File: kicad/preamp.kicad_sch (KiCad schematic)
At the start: 14 parts, among them Q1 MMBF5457, Q2 MMBF5457

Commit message: Datasheet footprints, floor-plan placement, headless autoroute (144/145, DRC 0)
PCB-AUDIT s1 fixes with datasheet-derived project footprints:
- TO-220-5_Vertical_P1.70mm_LM1875 (TI NDH0005D): 1.45 mm pads on the 1.1 mm
  drill -> 0.175 mm annular (was 0.0875, 5 DRC errors); pad-local 0.2 mm clearance
- Bridge_KBP_P3.81mm (Diodes DS39310 KBP404G-KBP410G, pins + ~ ~ -); bridge
  symbol renumbered to the physical order; errata #3 updated (KBU needs a swap)
- value-aware CP/R sizing (real can sizes for 4700/2200/1000 uF, 5 W / 1 W
  resistors, fat pads on the 0R speaker return); Part 4 wire pads for all
  off-board wiring (2.0 mm/1.2 mm signal, 3.0 mm/1.5 mm speaker + transformer)
- VRAW/AC1/AC2 moved into the HighCurrent net class (errata #11)

gen_pcb.py now places to the Part 5 floor plan: balanced columns (Input/Preamp
with Tone stacked below | Reverb/Trem/MRB | Power Amp | PSU), signal order inside
zones with serpentine shelves, LM1875/LM317 on the top edge with the 10 mm
keep-out, wiring edge along the bottom, 4x M3 holes, two locked 0.9 mm escape
stubs off the LM1875 pins 4/5 (a 1.5/2.5 mm trace cannot enter a 1.70 mm pitch).
DRC before routing: 0 errors, 0 warnings.

route_board.py: pcbnew DSN export -> Freerouting -> SES import -> pour refill.
Freerouting 2.1.0 ignores every pass/timeout limit in CLI mode and only writes
output at 0 unrouted (and its MT router crashed), so the script drives 1.9.0
under xvfb-run and injects autoroute_settings (bottom layer 6x cost, via 80) so
the GND pour stays whole. Committed board: 144/145 connections routed, 0 DRC
violations (--severity-all), 26 vias, 351 mm on the bottom vs 3.7 m on top; the
one open PA_OUT link (blocked by R_bias1) is documented as a GUI finish.

Chassis-fit figure corrected: the old 48-53 % / 82-90 % densities counted hidden
text boxes; text-less it is ~33 % on 190x115 and ~56 % on 155x90.

Docs: PCB-NOTES/PCB-AUDIT rewritten, README, CHANGELOG, errata #3/#11,
SOURCES (package drawings), Part 10, kicad RE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
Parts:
- C_s1, C_s2: footprint Capacitor_THT:CP_Radial_D8.0mm_P3.50mm -> Capacitor_THT:CP_Radial_D5.0mm_P2.00mm
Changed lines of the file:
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@@
     (pin "1")
     (pin "2")
-    (instances (project "cambridge_reverb" (path "/942ea049-022a-4522-9155-9a031f6385fe" (reference "C_in_pre") (unit 1))))
+    (instances (project "cambridge_reverb" (path "/0294f5b1-e3f0-489d-af89-80fb9260e410" (reference "C_in_pre") (unit 1))))
   )
   (wire (pts (xy 116.84 121.91999999999999) (xy 114.3 121.91999999999999)) (stroke (width 0) (type default)))
@@
     (pin "1")
     (pin "2")
-    (instances (project "cambridge_reverb" (path "/942ea049-022a-4522-9155-9a031f6385fe" (reference "R_g1") (unit 1))))
+    (instances (project "cambridge_reverb" (path "/0294f5b1-e3f0-489d-af89-80fb9260e410" (reference "R_g1") (unit 1))))
   )
   (wire (pts (xy 116.84 152.4) (xy 114.3 152.4)) (stroke (width 0) (type default)))
@@
     (pin "1")
     (pin "3")
-    (instances (project "cambridge_reverb" (path "/942ea049-022a-4522-9155-9a031f6385fe" (reference "Q1") (unit 1))))
+    (instances (project "cambridge_reverb" (path "/0294f5b1-e3f0-489d-af89-80fb9260e410" (reference "Q1") (unit 1))))
   )
   (wire (pts (xy 165.1 132.07999999999998) (xy 162.56 132.07999999999998)) (stroke (width 0) (type default)))
@@
     (pin "1")
     (pin "2")
-    (instances (project "cambridge_reverb" (path "/942ea049-022a-4522-9155-9a031f6385fe" (reference "R_d1") (unit 1))))
+    (instances (project "cambridge_reverb" (path "/0294f5b1-e3f0-489d-af89-80fb9260e410" (reference "R_d1") (unit 1))))
   )
   (wire (pts (xy 167.64 101.6) (xy 165.1 101.6)) (stroke (width 0) (type default)))
@@
     (pin "1")
     (pin "2")
-    (instances (project "cambridge_reverb" (path "/942ea049-022a-4522-9155-9a031f6385fe" (reference "R_s1") (unit 1))))
+    (instances (project "cambridge_reverb" (path "/0294f5b1-e3f0-489d-af89-80fb9260e410" (reference "R_s1") (unit 1))))
   )
   (wire (pts (xy 167.64 172.72) (xy 165.1 172.72)) (stroke (width 0) (type default)))
@@
     (property "Reference" "C_s1" (at 214.62999999999997 165.1 0) (effects (font (size 1.27 1.27)) (justify left)))
     (property "Value" "10uF/25V" (at 214.62999999999997 167.64 0) (effects (font (size 1.27 1.27)) (justify left)))
-    (property "Footprint" "Capacitor_THT:CP_Radial_D8.0mm_P3.50mm" (at 212.08999999999997 172.72 0) (effects (font (size 1.27 1.27)) hide))
+    (property "Footprint" "Capacitor_THT:CP_Radial_D5.0mm_P2.00mm" (at 212.08999999999997 172.72 0) (effects (font (size 1.27 1.27)) hide))
     (pin "1")
     (pin "2")
-    (instances (project "cambridge_reverb" (path "/942ea049-022a-4522-9155-9a031f6385fe" (reference "C_s1") (unit 1))))
+    (instances (project "cambridge_reverb" (path "/0294f5b1-e3f0-489d-af89-80fb9260e410" (reference "C_s1") (unit 1))))
   )
   (wire (pts (xy 207.01 172.72) (xy 204.46999999999997 172.72)) (stroke (width 0) (type default)))
@@
     (pin "1")
     (pin "2")
-    (instances (project "cambridge_reverb" (path "/942ea049-022a-4522-9155-9a031f6385fe" (reference "C_cpl12") (unit 1))))
+    (instances (project "cambridge_reverb" (path "/0294f5b1-e3f0-489d-af89-80fb9260e410" (reference "C_cpl12") (unit 1))))
   )
   (wire (pts (xy 207.01 132.07999999999998) (xy 204.46999999999997 132.07999999999998)) (stroke (width 0) (type default)))
@@
     (pin "1")
     (pin "2")
-    (instances (project "cambridge_reverb" (path "/942ea049-022a-4522-9155-9a031f6385fe" (reference "R_g2") (unit 1))))
+    (instances (project "cambridge_reverb" (path "/0294f5b1-e3f0-489d-af89-80fb9260e410" (reference "R_g2") (unit 1))))
   )
   (wire (pts (xy 207.01 157.48) (xy 204.46999999999997 157.48)) (stroke (width 0) (type default)))
@@
     (pin "1")
     (pin "3")
-    (instances (project "cambridge_reverb" (path "/942ea049-022a-4522-9155-9a031f6385fe" (reference "Q2") (unit 1))))
+    (instances (project "cambridge_reverb" (path "/0294f5b1-e3f0-489d-af89-80fb9260e410" (reference "Q2") (unit 1))))
   )
   (wire (pts (xy 250.19 132.07999999999998) (xy 247.64999999999998 132.07999999999998)) (stroke (width 0) (type default)))
@@
     (pin "1")
     (pin "2")
-    (instances (project "cambridge_reverb" (path "/942ea049-022a-4522-9155-9a031f6385fe" (reference "R_d2") (unit 1))))
+    (instances (project "cambridge_reverb" (path "/0294f5b1-e3f0-489d-af89-80fb9260e410" (reference "R_d2") (unit 1))))
   )
   (wire (pts (xy 252.72999999999996 101.6) (xy 250.19 101.6)) (stroke (width 0) (type default)))
@@
     (pin "1")
     (pin "2")
-    (instances (project "cambridge_reverb" (path "/942ea049-022a-4522-9155-9a031f6385fe" (reference "C_pres") (unit 1))))
+    (instances (project "cambridge_reverb" (path "/0294f5b1-e3f0-489d-af89-80fb9260e410" (reference "C_pres") (unit 1))))
   )
   (wire (pts (xy 252.72999999999996 172.72) (xy 250.19 172.72)) (stroke (width 0) (type default)))
@@
     (pin "1")
     (pin "2")
-    (instances (project "cambridge_reverb" (path "/942ea049-022a-4522-9155-9a031f6385fe" (reference "R_s2") (unit 1))))
+    (instances (project "cambridge_reverb" (path "/0294f5b1-e3f0-489d-af89-80fb9260e410" (reference "R_s2") (unit 1))))
   )
   (wire (pts (xy 292.09999999999997 157.48) (xy 289.56 157.48)) (stroke (width 0) (type default)))
@@
     (property "Reference" "C_s2" (at 299.72 173.98999999999998 0) (effects (font (size 1.27 1.27)) (justify left)))
     (property "Value" "10uF/25V" (at 299.72 176.52999999999997 0) (effects (font (size 1.27 1.27)) (justify left)))
-    (property "Footprint" "Capacitor_THT:CP_Radial_D8.0mm_P3.50mm" (at 297.18 181.60999999999999 0) (effects (font (size 1.27 1.27)) hide))
+    (property "Footprint" "Capacitor_THT:CP_Radial_D5.0mm_P2.00mm" (at 297.18 181.60999999999999 0) (effects (font (size 1.27 1.27)) hide))
     (pin "1")
     (pin "2")
-    (instances (project "cambridge_reverb" (path "/942ea049-022a-4522-9155-9a031f6385fe" (reference "C_s2") (unit 1))))
+    (instances (project "cambridge_reverb" (path "/0294f5b1-e3f0-489d-af89-80fb9260e410" (reference "C_s2") (unit 1))))
   )
   (wire (pts (xy 292.09999999999997 181.60999999999999) (xy 289.56 181.60999999999999)) (stroke (width 0) (type default)))
@@
     (pin "1")
     (pin "2")
-    (instances (project "cambridge_reverb" (path "/942ea049-022a-4522-9155-9a031f6385fe" (reference "C_treble") (unit 1))))
+    (instances (project "cambridge_reverb" (path "/0294f5b1-e3f0-489d-af89-80fb9260e410" (reference "C_treble") (unit 1))))
   )
   (wire (pts (xy 292.09999999999997 116.84) (xy 289.56 116.84)) (stroke (width 0) (type default)))

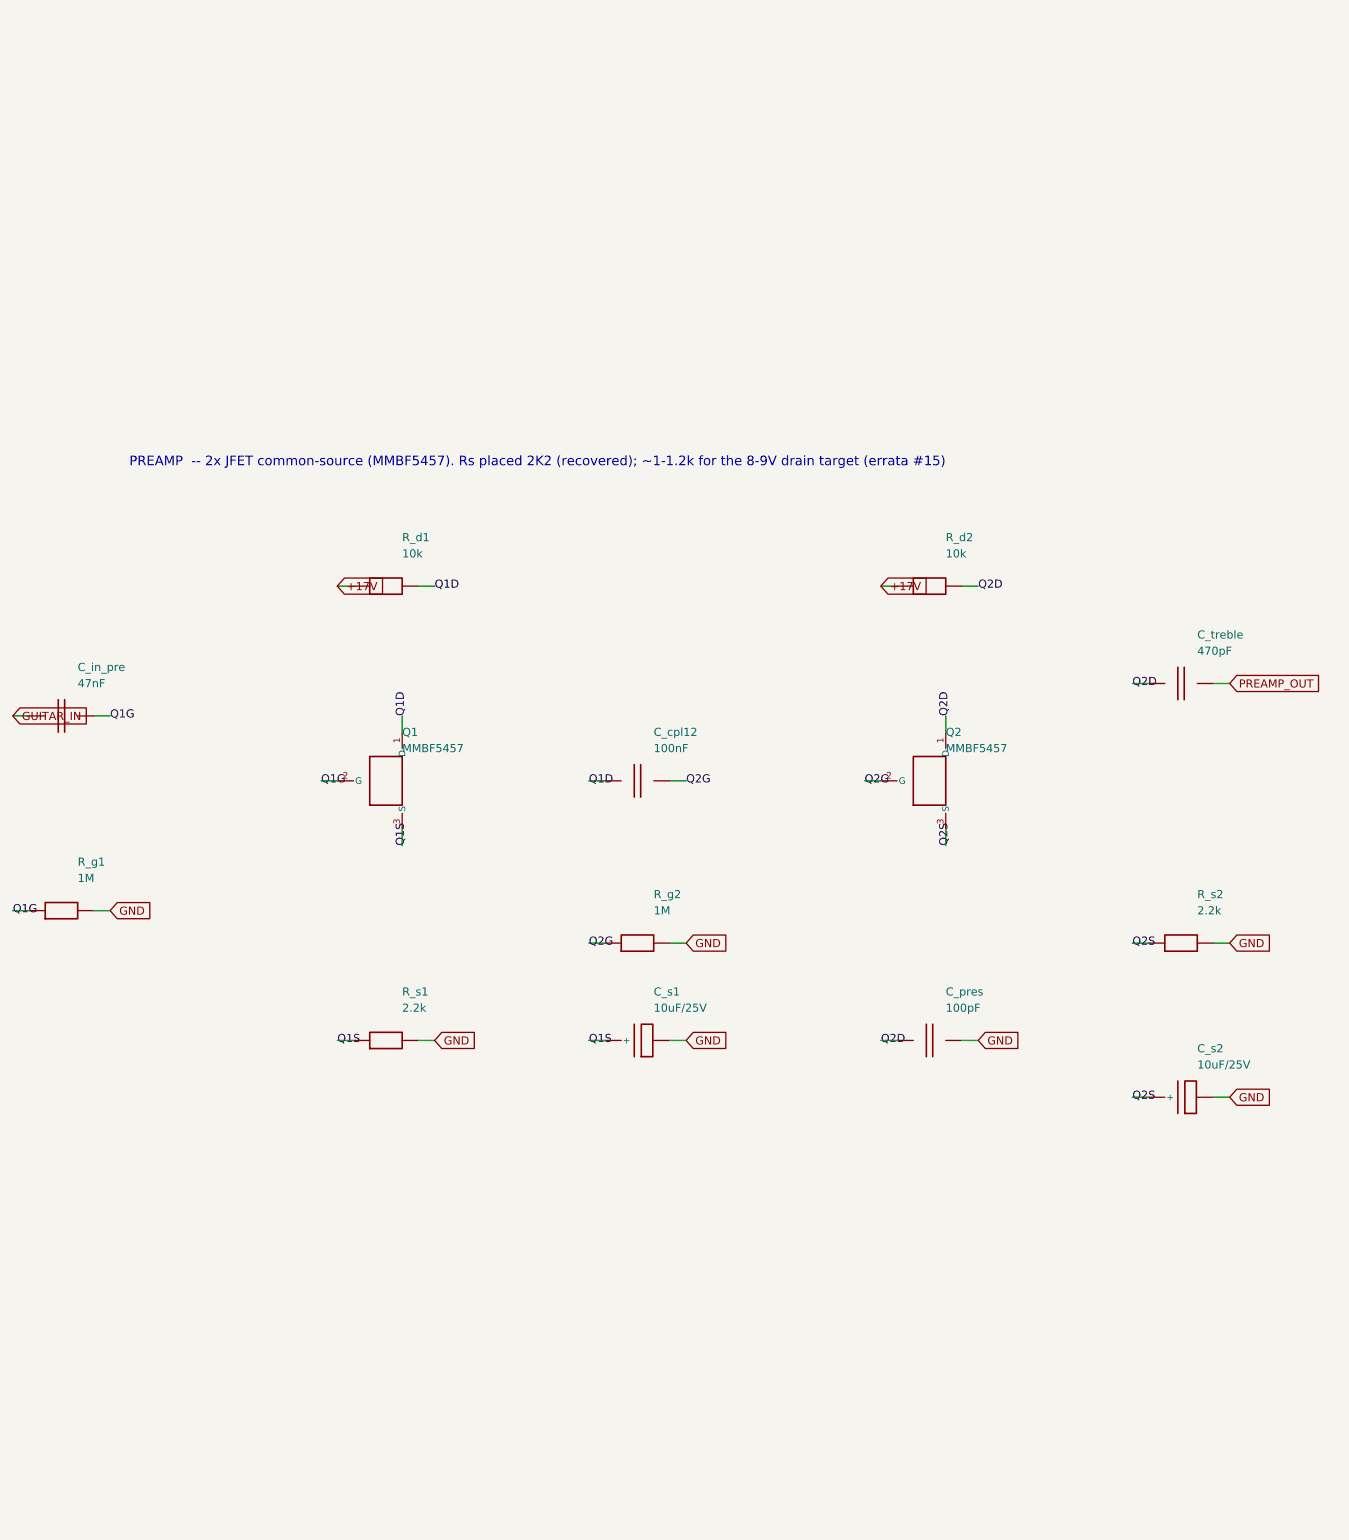
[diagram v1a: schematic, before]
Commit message: Add 26 labelled bench test points (schematic + BOM + silk) and re-route
Test points follow the Part 5 bring-up order: rails (VRAW, +33V5, VREG_IN,
+17V), JFET drains Q1D/Q2D/QRD (the errata #15 bias trim), the VBIAS_R/VBIAS_T
mid-rail refs, every inter-stage node (PREAMP_OUT, TONE_OUT, BLEND, TREM_OUT,
MRB_OUT, PA_IN), tank drive/return, LFO, PA_BIAS/PA_OUT/SPK_P, and a GND pin
per zone for the probe clip.

- gen_kicad.py: one-pin TP symbol; TEST_POINTS table; add_test_points() puts
  them on their sheets so they are in the netlist and the BOM (one order line)
- footprint TestPoint_THT_D2.0mm_Label: 2.0 mm pad / 1.0 mm drill for a header
  pin or wire loop; the footprint VALUE (= net alias) prints on F.SilkS
- gen_pcb.py: test-point strip across the top of each zone; the effects column
  is now two stacked zones (tremolo+MRB above, reverb below next to its tank
  pads) so each block's points sit right above its parts; stacked-zone gap 2 mm
- PCB-NOTES.md: test-point table with expected values (Part 3 troubleshooting,
  Part 2 set-up, ngspice) and the bring-up sequence
- Re-routed (Freerouting 1.9.0, B.Cu x7, via 60): 161/166 connections, 0 DRC
  violations, 54 vias; the five open links are listed for a GUI finish

Co-Authored-By: Claude Fable 5.1 <noreply@anthropic.com>
Claude-Session: https://claude.ai/code/session_01Vk8HkvCugxFpQsBPVnNT2H
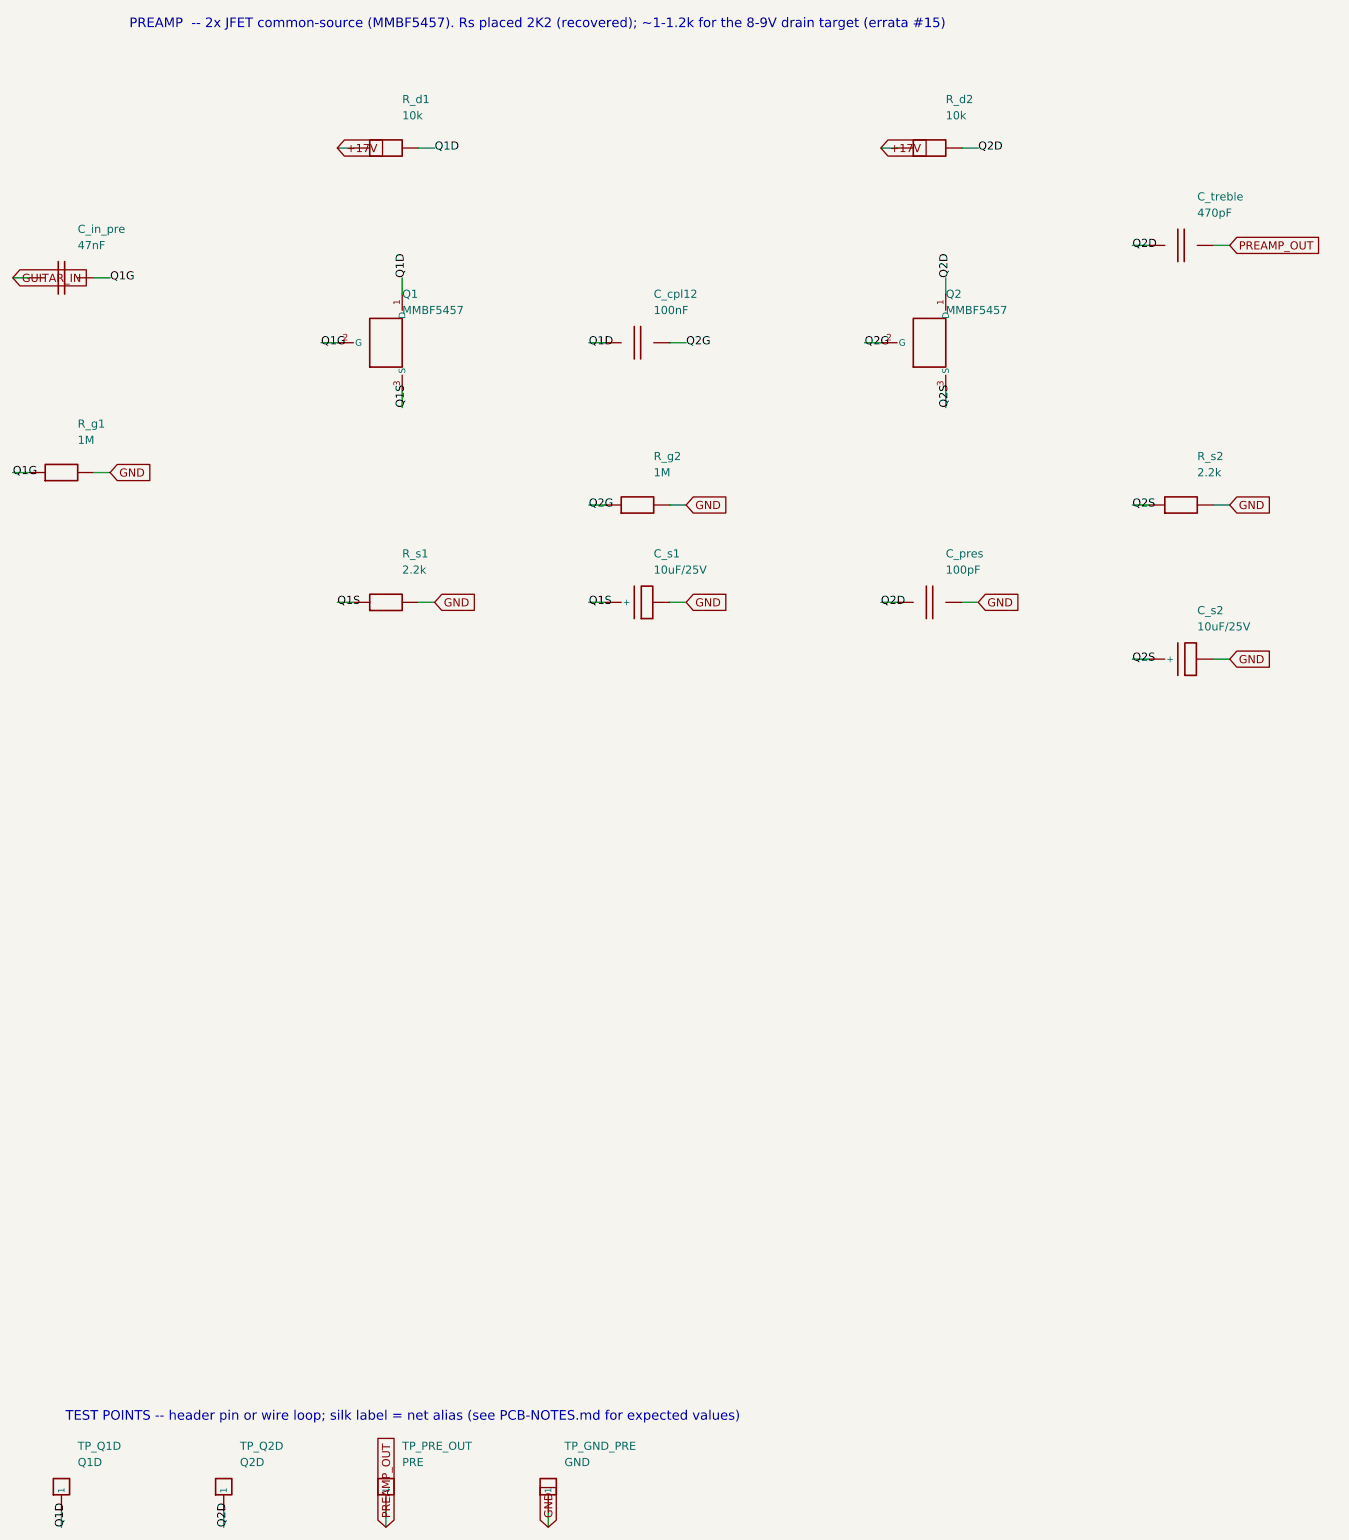
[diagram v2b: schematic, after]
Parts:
- added TP_GND_PRE: GND, cambridge_reverb:TestPoint_THT_D2.0mm_Label, symbol cr_primitives:TP
- added TP_PRE_OUT: PRE, cambridge_reverb:TestPoint_THT_D2.0mm_Label, symbol cr_primitives:TP
- added TP_Q1D: Q1D, cambridge_reverb:TestPoint_THT_D2.0mm_Label, symbol cr_primitives:TP
- added TP_Q2D: Q2D, cambridge_reverb:TestPoint_THT_D2.0mm_Label, symbol cr_primitives:TP
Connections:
- net GND: now also TP_GND_PRE.1
- net PREAMP_OUT: now also TP_PRE_OUT.1
- net Q1D: now also TP_Q1D.1
- net Q2D: now also TP_Q2D.1
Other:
- note added: "TEST POINTS -- header pin or wire loop; silk label = net alias (see PCB-NOTES.md for expected values)"
